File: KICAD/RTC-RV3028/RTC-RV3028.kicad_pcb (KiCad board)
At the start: 2 copper layers, 15.8 x 21.4 mm, 8 parts, among them J4 Conn_01x05_Male, Y1 RV-3028-C7_32.768kHz_1ppm_TA_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

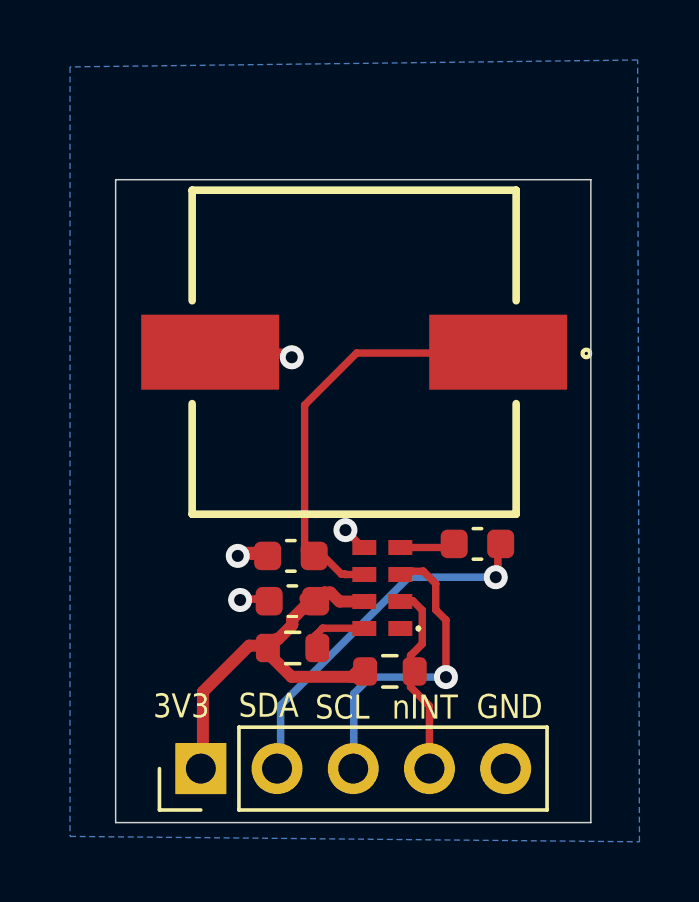
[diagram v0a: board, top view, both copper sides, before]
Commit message: corrected hibernate
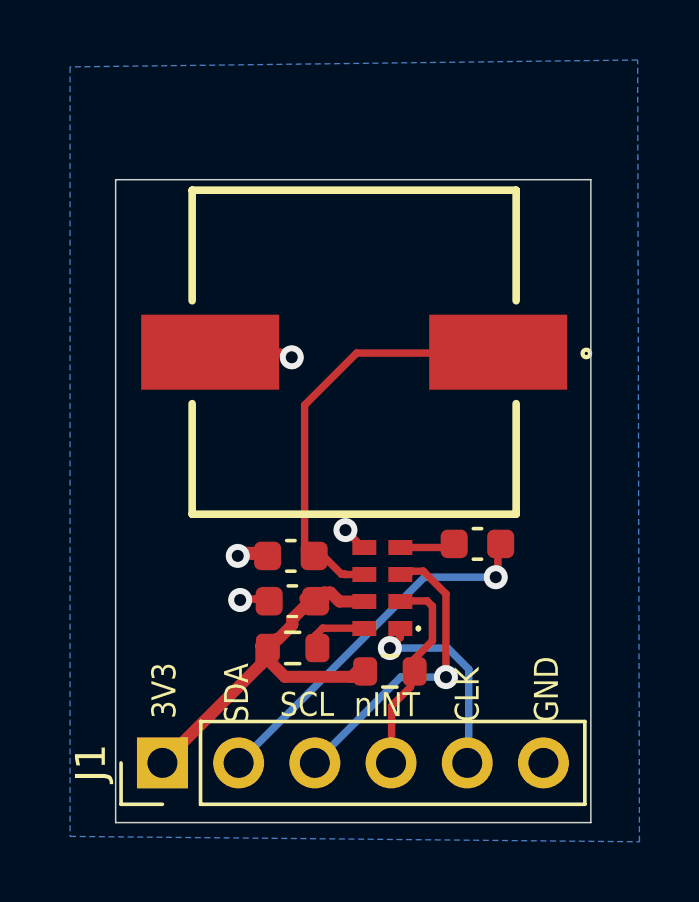
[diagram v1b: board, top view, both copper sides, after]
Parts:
- removed J4: Conn_01x05_Male, Connector_PinHeader_2.54mm:PinHeader_1x05_P2.54mm_Vertical
- added J1: Conn_01x06_Pin, Connector_PinHeader_2.54mm:PinHeader_1x06_P2.54mm_Vertical, F.Cu at (90.8, 112.4)
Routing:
- net /CLK: track 0.00 -> 6.86 mm, vias 0 -> 1
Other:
- board text added: "CLK"
